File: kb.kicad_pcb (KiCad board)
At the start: 2 copper layers, 1 part, among them U1 Pico

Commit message: laid out LEDs
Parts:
- added C1: C_Small, Capacitor_SMD:C_0805_2012Metric_Pad1.18x1.45mm_HandSolder, B.Cu at (-240.5, 34.1)
- added C10: C_Small, Capacitor_SMD:C_0805_2012Metric_Pad1.18x1.45mm_HandSolder, B.Cu at (-28.2, 154.1)
- added C11: C_Small, Capacitor_SMD:C_0805_2012Metric_Pad1.18x1.45mm_HandSolder, B.Cu at (-178.3, 93.5)
- added C12: C_Small, Capacitor_SMD:C_0805_2012Metric_Pad1.18x1.45mm_HandSolder, B.Cu at (-229.1, 44.8)
- added C13: C_Small, Capacitor_SMD:C_0805_2012Metric_Pad1.18x1.45mm_HandSolder, B.Cu at (-256.1, 18.6)
- added C14: C_Small, Capacitor_SMD:C_0805_2012Metric_Pad1.18x1.45mm_HandSolder, B.Cu at (-224.3, 44.8)
- added C15: C_Small, Capacitor_SMD:C_0805_2012Metric_Pad1.18x1.45mm_HandSolder, B.Cu at (-121.2, 152.3)
- added C16: C_Small, Capacitor_SMD:C_0805_2012Metric_Pad1.18x1.45mm_HandSolder, B.Cu at (-220.2, 51.3)
- added C17: C_Small, Capacitor_SMD:C_0805_2012Metric_Pad1.18x1.45mm_HandSolder, B.Cu at (-178.3, 96.5)
- added C18: C_Small, Capacitor_SMD:C_0805_2012Metric_Pad1.18x1.45mm_HandSolder, B.Cu at (-151.2, 122.9)
- added C19: C_Small, Capacitor_SMD:C_0805_2012Metric_Pad1.18x1.45mm_HandSolder, B.Cu at (-191.8, 85.5)
- added C2: C_Small, Capacitor_SMD:C_0805_2012Metric_Pad1.18x1.45mm_HandSolder, B.Cu at (-180.3, 90.5)
- added C20: C_Small, Capacitor_SMD:C_0805_2012Metric_Pad1.18x1.45mm_HandSolder, B.Cu at (-235.8, 37.8)
- added C21: C_Small, Capacitor_SMD:C_0805_2012Metric_Pad1.18x1.45mm_HandSolder, B.Cu at (-173.5, 102.4)
- added C22: C_Small, Capacitor_SMD:C_0805_2012Metric_Pad1.18x1.45mm_HandSolder, B.Cu at (-18.5, 154.1)
- added C23: C_Small, Capacitor_SMD:C_0805_2012Metric_Pad1.18x1.45mm_HandSolder, B.Cu at (-129.0, 146.1)
- added C24: C_Small, Capacitor_SMD:C_0805_2012Metric_Pad1.18x1.45mm_HandSolder, B.Cu at (-205.9, 66.9)
- added C25: C_Small, Capacitor_SMD:C_0805_2012Metric_Pad1.18x1.45mm_HandSolder, B.Cu at (-159.9, 110.7)
- added C26: C_Small, Capacitor_SMD:C_0805_2012Metric_Pad1.18x1.45mm_HandSolder, B.Cu at (-23.3, 154.1)
- added C27: C_Small, Capacitor_SMD:C_0805_2012Metric_Pad1.18x1.45mm_HandSolder, B.Cu at (-153.3, 119.6)
- added C28: C_Small, Capacitor_SMD:C_0805_2012Metric_Pad1.18x1.45mm_HandSolder, B.Cu at (-191.8, 82.5)
- added C29: C_Small, Capacitor_SMD:C_0805_2012Metric_Pad1.18x1.45mm_HandSolder, B.Cu at (-240.5, 31.1)
- added C3: C_Small, Capacitor_SMD:C_0805_2012Metric_Pad1.18x1.45mm_HandSolder, B.Cu at (-159.9, 113.7)
- added C30: C_Small, Capacitor_SMD:C_0805_2012Metric_Pad1.18x1.45mm_HandSolder, B.Cu at (-164.7, 113.7)
- added C31: C_Small, Capacitor_SMD:C_0805_2012Metric_Pad1.18x1.45mm_HandSolder, B.Cu at (-144.5, 130.9)
- added C32: C_Small, Capacitor_SMD:C_0805_2012Metric_Pad1.18x1.45mm_HandSolder, B.Cu at (-164.7, 110.7)
- added C33: C_Small, Capacitor_SMD:C_0805_2012Metric_Pad1.18x1.45mm_HandSolder, B.Cu at (-173.5, 96.3)
- added C34: C_Small, Capacitor_SMD:C_0805_2012Metric_Pad1.18x1.45mm_HandSolder, B.Cu at (-205.9, 69.9)
- added C35: C_Small, Capacitor_SMD:C_0805_2012Metric_Pad1.18x1.45mm_HandSolder, B.Cu at (-173.5, 99.3)
- added C36: C_Small, Capacitor_SMD:C_0805_2012Metric_Pad1.18x1.45mm_HandSolder, B.Cu at (-145.5, 127.5)
- added C37: C_Small, Capacitor_SMD:C_0805_2012Metric_Pad1.18x1.45mm_HandSolder, B.Cu at (-185.1, 90.5)
- added C38: C_Small, Capacitor_SMD:C_0805_2012Metric_Pad1.18x1.45mm_HandSolder, B.Cu at (-129.0, 143.1)
- added C39: C_Small, Capacitor_SMD:C_0805_2012Metric_Pad1.18x1.45mm_HandSolder, B.Cu at (-200.2, 74.5)
- added C4: C_Small, Capacitor_SMD:C_0805_2012Metric_Pad1.18x1.45mm_HandSolder, B.Cu at (-215.8, 59.3)
- added C40: C_Small, Capacitor_SMD:C_0805_2012Metric_Pad1.18x1.45mm_HandSolder, B.Cu at (-200.2, 71.5)
- added C41: C_Small, Capacitor_SMD:C_0805_2012Metric_Pad1.18x1.45mm_HandSolder, B.Cu at (-139.7, 133.9)
- added C42: C_Small, Capacitor_SMD:C_0805_2012Metric_Pad1.18x1.45mm_HandSolder, B.Cu at (-183.1, 93.5)
- added C43: C_Small, Capacitor_SMD:C_0805_2012Metric_Pad1.18x1.45mm_HandSolder, B.Cu at (-246.2, 29.5)
- added C44: C_Small, Capacitor_SMD:C_0805_2012Metric_Pad1.18x1.45mm_HandSolder, B.Cu at (-246.2, 26.5)
- added C5: C_Small, Capacitor_SMD:C_0805_2012Metric_Pad1.18x1.45mm_HandSolder, B.Cu at (-186.0, 87.1)
- added C6: C_Small, Capacitor_SMD:C_0805_2012Metric_Pad1.18x1.45mm_HandSolder, B.Cu at (-165.7, 107.6)
- added C7: C_Small, Capacitor_SMD:C_0805_2012Metric_Pad1.18x1.45mm_HandSolder, B.Cu at (-139.7, 130.9)
- added C8: C_Small, Capacitor_SMD:C_0805_2012Metric_Pad1.18x1.45mm_HandSolder, B.Cu at (-138.8, 139.8)
- added C9: C_Small, Capacitor_SMD:C_0805_2012Metric_Pad1.18x1.45mm_HandSolder, B.Cu at (-228.0, 47.8)
- added D0: D_Small, Diode_SMD:D_SOD-123, B.Cu at (-230.5, 38.2)
- added D1: D_Small, Diode_SMD:D_SOD-123, B.Cu at (-209.2, 52.8)
- added D10: D_Small, Diode_SMD:D_SOD-123, B.Cu at (-140.2, 127.7)
- added D101: SK6812MINI, Keebio-Parts:SK6812-MINI-E, B.Cu at (56.4, 77.0)
- added D102: SK6812MINI, Keebio-Parts:SK6812-MINI-E, B.Cu at (75.4, 77.0)
- added D103: SK6812MINI, Keebio-Parts:SK6812-MINI-E, B.Cu at (99.2, 77.0)
- added D104: SK6812MINI, Keebio-Parts:SK6812-MINI-E, B.Cu at (118.3, 77.0)
- added D105: SK6812MINI, Keebio-Parts:SK6812-MINI-E, B.Cu at (137.3, 77.0)
- added D106: SK6812MINI, Keebio-Parts:SK6812-MINI-E, B.Cu at (156.4, 77.0)
- added D107: SK6812MINI, Keebio-Parts:SK6812-MINI-E, B.Cu at (175.4, 77.0)
- added D108: SK6812MINI, Keebio-Parts:SK6812-MINI-E, B.Cu at (194.5, 77.0)
- added D109: SK6812MINI, Keebio-Parts:SK6812-MINI-E, B.Cu at (37.3, 96.0)
- added D11: D_Small, Diode_SMD:D_SOD-123, B.Cu at (-123.8, 144.5)
- added D110: SK6812MINI, Keebio-Parts:SK6812-MINI-E, B.Cu at (56.4, 96.0)
- added D111: SK6812MINI, Keebio-Parts:SK6812-MINI-E, B.Cu at (75.4, 96.0)
- added D112: SK6812MINI, Keebio-Parts:SK6812-MINI-E, B.Cu at (104.0, 96.0)
- added D113: SK6812MINI, Keebio-Parts:SK6812-MINI-E, B.Cu at (127.8, 96.0)
- added D114: SK6812MINI, Keebio-Parts:SK6812-MINI-E, B.Cu at (146.8, 96.0)
- added D115: SK6812MINI, Keebio-Parts:SK6812-MINI-E, B.Cu at (165.9, 96.0)
- added D116: SK6812MINI, Keebio-Parts:SK6812-MINI-E, B.Cu at (184.9, 96.0)
- added D117: SK6812MINI, Keebio-Parts:SK6812-MINI-E, B.Cu at (204.0, 96.0)
- added D118: SK6812MINI, Keebio-Parts:SK6812-MINI-E, B.Cu at (37.3, 115.1)
- added D119: SK6812MINI, Keebio-Parts:SK6812-MINI-E, B.Cu at (56.4, 115.1)
- added D12: D_Small, Diode_SMD:D_SOD-123, B.Cu at (-146.0, 124.3)
- added D120: SK6812MINI, Keebio-Parts:SK6812-MINI-E, B.Cu at (75.4, 115.1)
- added D121: SK6812MINI, Keebio-Parts:SK6812-MINI-E, B.Cu at (106.4, 115.1)
- added D122: SK6812MINI, Keebio-Parts:SK6812-MINI-E, B.Cu at (132.6, 115.1)
- added D123: SK6812MINI, Keebio-Parts:SK6812-MINI-E, B.Cu at (151.6, 115.1)
- added D124: SK6812MINI, Keebio-Parts:SK6812-MINI-E, B.Cu at (170.7, 115.1)
- added D125: SK6812MINI, Keebio-Parts:SK6812-MINI-E, B.Cu at (189.7, 115.1)
- added D126: SK6812MINI, Keebio-Parts:SK6812-MINI-E, B.Cu at (208.8, 115.1)
- added D127: SK6812MINI, Keebio-Parts:SK6812-MINI-E, B.Cu at (37.3, 134.1)
- added D128: SK6812MINI, Keebio-Parts:SK6812-MINI-E, B.Cu at (56.4, 134.1)
- added D129: SK6812MINI, Keebio-Parts:SK6812-MINI-E, B.Cu at (75.4, 134.1)
- added D13: D_Small, Diode_SMD:D_SOD-123, B.Cu at (-168.2, 101.1)
- added D130: SK6812MINI, Keebio-Parts:SK6812-MINI-E, B.Cu at (111.1, 134.1)
- added D131: SK6812MINI, Keebio-Parts:SK6812-MINI-E, B.Cu at (142.1, 134.1)
- added D132: SK6812MINI, Keebio-Parts:SK6812-MINI-E, B.Cu at (161.1, 134.1)
- added D133: SK6812MINI, Keebio-Parts:SK6812-MINI-E, B.Cu at (180.2, 134.1)
- added D134: SK6812MINI, Keebio-Parts:SK6812-MINI-E, B.Cu at (199.2, 134.1)
- added D135: SK6812MINI, Keebio-Parts:SK6812-MINI-E, B.Cu at (218.3, 134.1)
- added D136: SK6812MINI, Keebio-Parts:SK6812-MINI-E, B.Cu at (37.3, 153.2)
- added D137: SK6812MINI, Keebio-Parts:SK6812-MINI-E, B.Cu at (56.4, 153.2)
- added D138: SK6812MINI, Keebio-Parts:SK6812-MINI-E, B.Cu at (75.4, 153.2)
- added D139: SK6812MINI, Keebio-Parts:SK6812-MINI-E, B.Cu at (104.0, 153.2)
- added D14: D_Small, Diode_SMD:D_SOD-123, B.Cu at (-168.2, 97.8)
- added D140: SK6812MINI, Keebio-Parts:SK6812-MINI-E, B.Cu at (130.2, 153.2)
- added D141: SK6812MINI, Keebio-Parts:SK6812-MINI-E, B.Cu at (154.0, 153.2)
- added D142: SK6812MINI, Keebio-Parts:SK6812-MINI-E, B.Cu at (177.8, 153.2)
- added D143: SK6812MINI, Keebio-Parts:SK6812-MINI-E, B.Cu at (208.8, 153.2)
- added D144: SK6812MINI, Keebio-Parts:SK6812-MINI-E, B.Cu at (213.5, 77.0)
- added D15: D_Small, Diode_SMD:D_SOD-123, B.Cu at (-140.2, 124.3)
- added D16: D_Small, Diode_SMD:D_SOD-123, B.Cu at (-173.0, 93.2)
- added D17: D_Small, Diode_SMD:D_SOD-123, B.Cu at (-116.0, 152.5)
- added D18: D_Small, Diode_SMD:D_SOD-123, B.Cu at (-127.8, 139.9)
- added D19: D_Small, Diode_SMD:D_SOD-123, B.Cu at (-235.2, 31.3)
- added D2: D_Small, Diode_SMD:D_SOD-123, B.Cu at (-186.5, 83.9)
- added D20: D_Small, Diode_SMD:D_SOD-123, B.Cu at (-230.5, 41.6)
- added D21: D_Small, Diode_SMD:D_SOD-123, B.Cu at (-214.9, 52.8)
- added D22: D_Small, Diode_SMD:D_SOD-123, B.Cu at (-116.0, 149.1)
- added D23: D_Small, Diode_SMD:D_SOD-123, B.Cu at (-235.2, 27.9)
- added D24: D_Small, Diode_SMD:D_SOD-123, B.Cu at (-180.8, 83.9)
- added D25: D_Small, Diode_SMD:D_SOD-123, B.Cu at (-180.8, 87.3)
- added D26: D_Small, Diode_SMD:D_SOD-123, B.Cu at (-210.5, 56.1)
- added D27: D_Small, Diode_SMD:D_SOD-123, B.Cu at (-222.7, 48.1)
- added D28: D_Small, Diode_SMD:D_SOD-123, B.Cu at (-217.0, 48.1)
- added D29: D_Small, Diode_SMD:D_SOD-123, B.Cu at (-133.6, 139.9)
- added D3: D_Small, Diode_SMD:D_SOD-123, B.Cu at (-160.4, 107.5)
- added D30: D_Small, Diode_SMD:D_SOD-123, B.Cu at (-216.2, 56.1)
- added D31: D_Small, Diode_SMD:D_SOD-123, B.Cu at (-194.9, 78.4)
- added D32: D_Small, Diode_SMD:D_SOD-123, B.Cu at (-166.2, 104.5)
- added D33: D_Small, Diode_SMD:D_SOD-123, B.Cu at (-250.8, 22.1)
- added D34: D_Small, Diode_SMD:D_SOD-123, B.Cu at (-188.6, 79.3)
- added D35: D_Small, Diode_SMD:D_SOD-123, B.Cu at (-235.2, 34.6)
- added D36: D_Small, Diode_SMD:D_SOD-123, B.Cu at (-148.0, 119.7)
- added D37: D_Small, Diode_SMD:D_SOD-123, B.Cu at (-160.4, 104.1)
- added D38: D_Small, Diode_SMD:D_SOD-123, B.Cu at (-194.9, 75.0)
- added D39: D_Small, Diode_SMD:D_SOD-123, B.Cu at (-241.0, 27.9)
- added D4: D_Small, Diode_SMD:D_SOD-123, B.Cu at (-200.6, 68.3)
- added D40: D_Small, Diode_SMD:D_SOD-123, B.Cu at (-250.8, 18.7)
- added D41: D_Small, Diode_SMD:D_SOD-123, B.Cu at (-210.5, 59.5)
- added D42: D_Small, Diode_SMD:D_SOD-123, B.Cu at (-224.8, 41.6)
- added D43: D_Small, Diode_SMD:D_SOD-123, B.Cu at (-224.8, 38.2)
- added D44: D_Small, Diode_SMD:D_SOD-123, B.Cu at (-202.7, 63.7)
- added D5: D_Small, Diode_SMD:D_SOD-123, B.Cu at (-194.9, 71.7)
- added D6: D_Small, Diode_SMD:D_SOD-123, B.Cu at (-243.0, 23.3)
- added D7: D_Small, Diode_SMD:D_SOD-123, B.Cu at (-210.5, 62.8)
- added D8: D_Small, Diode_SMD:D_SOD-123, B.Cu at (-121.7, 149.1)
- added D9: D_Small, Diode_SMD:D_SOD-123, B.Cu at (-194.9, 68.3)
- added J1: Conn_01x04_Female, Connector_PinSocket_2.54mm:PinSocket_1x04_P2.54mm_Vertical, F.Cu at (-53.2, -29.2)
- added J2: 10029449-001RLF, 10029449-001RLF:AMPHENOL_10029449-001RLF, B.Cu at (-25.7, 143.3)
- added MX1: MX-NoLED, MX_Only:MXOnly-1U-Hotswap, F.Cu at (56.4, 71.4)
- added MX10: MX-NoLED, MX_Only:MXOnly-1U-Hotswap, F.Cu at (56.4, 90.5)
- added MX11: MX-NoLED, MX_Only:MXOnly-1U-Hotswap, F.Cu at (75.4, 90.5)
- added MX12: MX-NoLED, MX_Only:MXOnly-1.5U-Hotswap, F.Cu at (104.0, 90.5)
- added MX13: MX-NoLED, MX_Only:MXOnly-1U-Hotswap, F.Cu at (127.8, 90.5)
- added MX14: MX-NoLED, MX_Only:MXOnly-1U-Hotswap, F.Cu at (146.8, 90.5)
- added MX15: MX-NoLED, MX_Only:MXOnly-1U-Hotswap, F.Cu at (165.9, 90.5)
- added MX16: MX-NoLED, MX_Only:MXOnly-1U-Hotswap, F.Cu at (184.9, 90.5)
- added MX17: MX-NoLED, MX_Only:MXOnly-1U-Hotswap, F.Cu at (204.0, 90.5)
- added MX18: MX-NoLED, MX_Only:MXOnly-1U-Hotswap, F.Cu at (37.3, 109.5)
- added MX19: MX-NoLED, MX_Only:MXOnly-1U-Hotswap, F.Cu at (56.4, 109.5)
- added MX2: MX-NoLED, MX_Only:MXOnly-1U-Hotswap, F.Cu at (75.4, 71.4)
- added MX20: MX-NoLED, MX_Only:MXOnly-1U-Hotswap, F.Cu at (75.4, 109.5)
- added MX21: MX-NoLED, MX_Only:MXOnly-1.75U-Hotswap, F.Cu at (106.4, 109.5)
- added MX22: MX-NoLED, MX_Only:MXOnly-1U-Hotswap, F.Cu at (132.6, 109.5)
- added MX23: MX-NoLED, MX_Only:MXOnly-1U-Hotswap, F.Cu at (151.6, 109.5)
- added MX24: MX-NoLED, MX_Only:MXOnly-1U-Hotswap, F.Cu at (170.7, 109.5)
- added MX25: MX-NoLED, MX_Only:MXOnly-1U-Hotswap, F.Cu at (189.7, 109.5)
- added MX26: MX-NoLED, MX_Only:MXOnly-1U-Hotswap, F.Cu at (208.8, 109.5)
- added MX27: MX-NoLED, MX_Only:MXOnly-1U-Hotswap, F.Cu at (37.3, 128.6)
- added MX28: MX-NoLED, MX_Only:MXOnly-1U-Hotswap, F.Cu at (56.4, 128.6)
- added MX29: MX-NoLED, MX_Only:MXOnly-1U-Hotswap, F.Cu at (75.4, 128.6)
- added MX3: MX-NoLED, MX_Only:MXOnly-1U-Hotswap, F.Cu at (99.2, 71.4)
- added MX30: MX-NoLED, MX_Only:MXOnly-2.25U-Hotswap, F.Cu at (111.1, 128.6)
- added MX31: MX-NoLED, MX_Only:MXOnly-1U-Hotswap, F.Cu at (142.1, 128.6)
- added MX32: MX-NoLED, MX_Only:MXOnly-1U-Hotswap, F.Cu at (161.1, 128.6)
- added MX33: MX-NoLED, MX_Only:MXOnly-1U-Hotswap, F.Cu at (180.2, 128.6)
- added MX34: MX-NoLED, MX_Only:MXOnly-1U-Hotswap, F.Cu at (199.2, 128.6)
- added MX35: MX-NoLED, MX_Only:MXOnly-1U-Hotswap, F.Cu at (218.3, 128.6)
- added MX36: MX-NoLED, MX_Only:MXOnly-1U-Hotswap, F.Cu at (37.3, 147.6)
- added MX37: MX-NoLED, MX_Only:MXOnly-1U-Hotswap, F.Cu at (56.4, 147.6)
- added MX38: MX-NoLED, MX_Only:MXOnly-1U-Hotswap, F.Cu at (75.4, 147.6)
- added MX39: MX-NoLED, MX_Only:MXOnly-1.5U-Hotswap, F.Cu at (104.0, 147.6)
- added MX4: MX-NoLED, MX_Only:MXOnly-1U-Hotswap, F.Cu at (118.3, 71.4)
- added MX40: MX-NoLED, MX_Only:MXOnly-1.25U-Hotswap, F.Cu at (130.2, 147.6)
- added MX41: MX-NoLED, MX_Only:MXOnly-1.25U-Hotswap, F.Cu at (154.0, 147.6)
- added MX42: MX-NoLED, MX_Only:MXOnly-1.25U-Hotswap, F.Cu at (177.8, 147.6)
- added MX43: MX-NoLED, MX_Only:MXOnly-2U-Hotswap, F.Cu at (208.8, 147.6)
- added MX44: MX-NoLED, MX_Only:MXOnly-1U-Hotswap, F.Cu at (213.5, 71.4)
- added MX5: MX-NoLED, MX_Only:MXOnly-1U-Hotswap, F.Cu at (137.3, 71.4)
- added MX6: MX-NoLED, MX_Only:MXOnly-1U-Hotswap, F.Cu at (156.4, 71.4)
- added MX7: MX-NoLED, MX_Only:MXOnly-1U-Hotswap, F.Cu at (175.4, 71.4)
- added MX8: MX-NoLED, MX_Only:MXOnly-1U-Hotswap, F.Cu at (194.5, 71.4)
- added MX9: MX-NoLED, MX_Only:MXOnly-1U-Hotswap, F.Cu at (37.3, 90.5)
- added SW1: RotaryEncoder_Switch, Keebio-Parts:RotaryEncoder_EC11, F.Cu at (33.3, 67.5)
- added U2: SN74AHCT125D, Package_DIP:DIP-14_W7.62mm_Socket, F.Cu at (-71.3, -33.8)
- moved U1 30.2 mm to (49.2, 25.4), turned to 90 degrees
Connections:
- U1 pad 13: unconnected-(U1-Pad13) -> GND
- U1 pad 18: unconnected-(U1-Pad18) -> GND
- U1 pad 3: unconnected-(U1-Pad3) -> GND
- U1 pad 40: unconnected-(U1-Pad40) -> +5V
- U1 pad 42: unconnected-(U1-Pad42) -> GND
- U1 pad 8: unconnected-(U1-Pad8) -> GND
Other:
- board outline added: 3.4 x 3 mm

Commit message: layout nearly finished
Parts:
- U1: moved to B.Cu
- moved D35 471.3 mm to (225.4, 134.1), turned to 90 degrees
- moved C43 464.6 mm to (201.6, 153.2), turned to 90 degrees
- moved D43 455.4 mm to (215.9, 153.2), turned to 90 degrees
- moved C44 455.4 mm to (206.4, 77.0), turned to 90 degrees
- moved D33 452.2 mm to (187.3, 134.1), turned to 90 degrees
- moved D26 430.4 mm to (215.9, 115.1), turned to 90 degrees
- moved D42 424.6 mm to (184.9, 153.2), turned to 90 degrees
- moved D44 423.6 mm to (220.7, 77.0), turned to 90 degrees
- moved D40 410.8 mm to (137.3, 153.2), turned to 90 degrees
- moved D6 410.0 mm to (163.5, 77.0), turned to 90 degrees
- moved D23 403.5 mm to (158.8, 115.1), turned to 90 degrees
- moved C34 403.1 mm to (192.1, 134.1), turned to 90 degrees
- moved C16 400.5 mm to (177.8, 96.0), turned to 90 degrees
- moved D34 398.7 mm to (206.4, 134.1), turned to 90 degrees
- moved D7 393.3 mm to (182.6, 77.0), turned to 90 degrees
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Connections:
- D103 pad 1: Net-(D103-Pad1) -> (no net)
- D103 pad 2: GND -> (no net)
- D103 pad 3: Net-(D102-Pad1) -> (no net)
- D103 pad 4: +5V -> (no net)
- D115 pad 1: Net-(D115-Pad1) -> (no net)
- D115 pad 2: GND -> (no net)
- D115 pad 3: Net-(D114-Pad1) -> (no net)
- D115 pad 4: +5V -> (no net)
- D29 pad 1: /ROW3 -> (no net)
- D29 pad 2: Net-(MX29-Pad2) -> (no net)
- D34 pad 1: /ROW3 -> (no net)
- D34 pad 2: Net-(MX34-Pad2) -> (no net)
- MX9 pad 1: /COL0 -> (no net)
- MX9 pad 2: Net-(MX9-Pad2) -> (no net)

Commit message: about to start routing
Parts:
- U2: footprint Package_DIP:DIP-14_W7.62mm_Socket -> Package_SO:TSSOP-14-1EP_4.4x5mm_P0.65mm; moved to B.Cu
- moved U1 40.5 mm to (61.9, 66.7)
- moved U2 13.2 mm to (77.8, 44.5), turned to 180 degrees
- moved J2 2.30 mm to (101.2, 52.4), turned to -90 degrees
- moved C1 1.59 mm to (49.2, 70.6)
- moved C2 1.59 mm to (68.3, 70.6)
- moved D0 1.59 mm to (44.5, 70.6)
- moved D1 1.59 mm to (63.5, 70.6)
- moved D2 1.59 mm to (82.5, 70.6)
- moved J1 0.79 mm to (91.3, 52.2)
- turned SW1 to 180 degrees
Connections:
- D101 pad 3: unconnected-(D101-Pad3) -> /RGB_5V
- D103 pad 1: (no net) -> Net-(D103-Pad1)
- D103 pad 2: (no net) -> GND
- D103 pad 3: (no net) -> Net-(D102-Pad1)
- D103 pad 4: (no net) -> +5V
- D108 pad 1: unconnected-(D108-Pad1) -> Net-(D109-Pad3)
- D109 pad 3: unconnected-(D109-Pad3) -> Net-(D109-Pad3)
- D115 pad 1: (no net) -> Net-(D115-Pad1)
- D115 pad 2: (no net) -> GND
- D115 pad 3: (no net) -> Net-(D114-Pad1)
- D115 pad 4: (no net) -> +5V
- D117 pad 1: unconnected-(D117-Pad1) -> Net-(D118-Pad3)
- D118 pad 3: unconnected-(D118-Pad3) -> Net-(D118-Pad3)
- D126 pad 1: unconnected-(D126-Pad1) -> Net-(D127-Pad3)
- D127 pad 3: unconnected-(D127-Pad3) -> Net-(D127-Pad3)
- D135 pad 1: unconnected-(D135-Pad1) -> Net-(D136-Pad3)
- D136 pad 3: unconnected-(D136-Pad3) -> Net-(D136-Pad3)
- D144 pad 1: unconnected-(D144-Pad1) -> /RGB_TO_RIGHT
- D29 pad 1: (no net) -> /ROW3
- D29 pad 2: (no net) -> Net-(D29-Pad2)
- D34 pad 1: (no net) -> /ROW3
- D34 pad 2: (no net) -> Net-(D34-Pad2)
- D9 pad 2: Net-(MX9-Pad2) -> Net-(D9-Pad2)
- MX29 pad 2: Net-(MX29-Pad2) -> Net-(D29-Pad2)
- MX34 pad 2: Net-(MX34-Pad2) -> Net-(D34-Pad2)
- MX9 pad 1: (no net) -> /COL0
- MX9 pad 2: (no net) -> Net-(D9-Pad2)

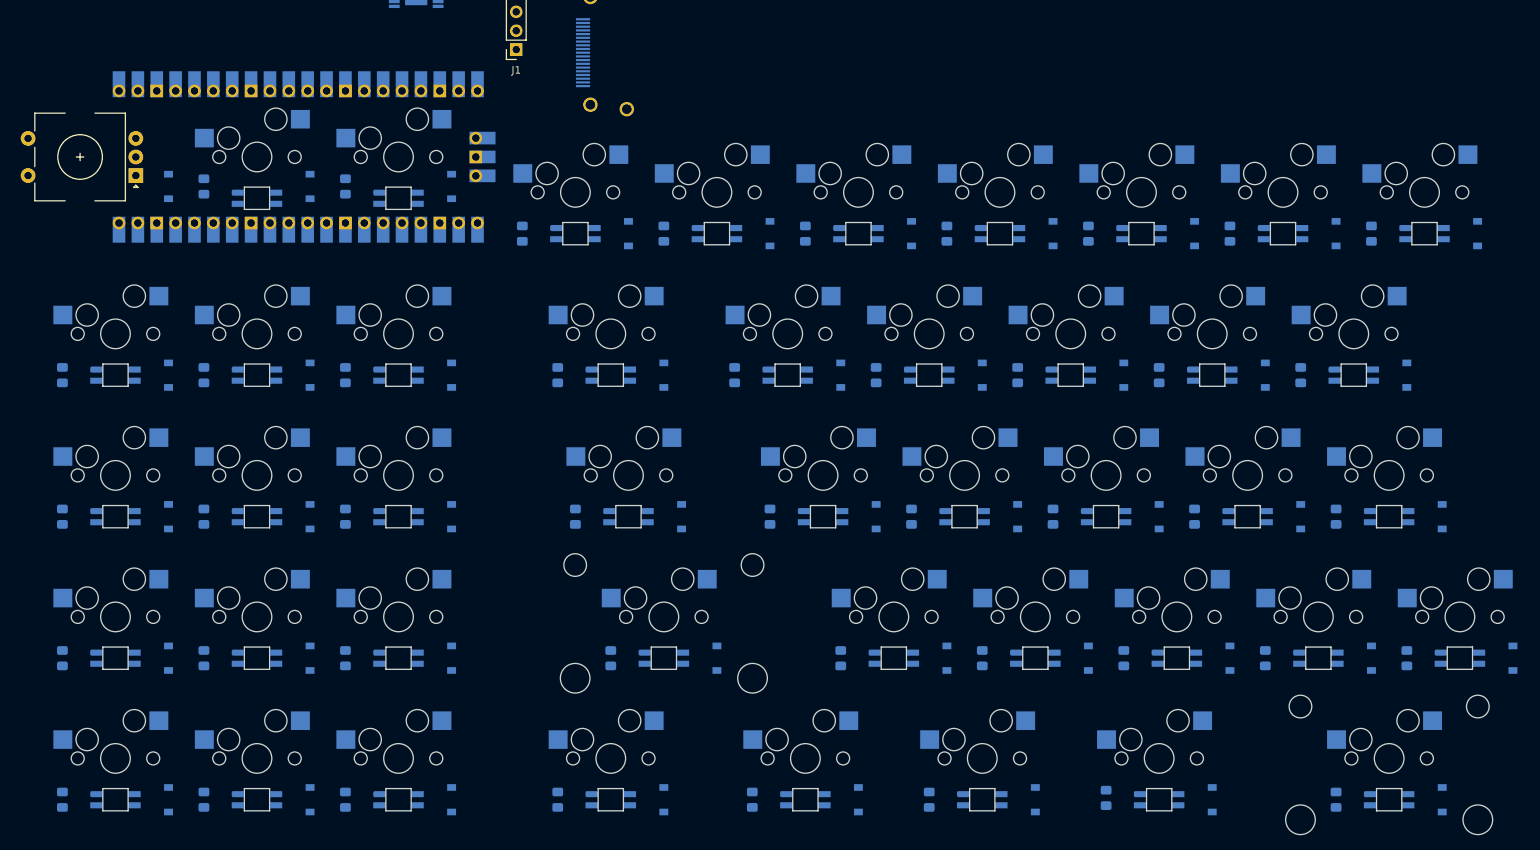
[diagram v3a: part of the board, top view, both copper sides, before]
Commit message: cols 3-8 done
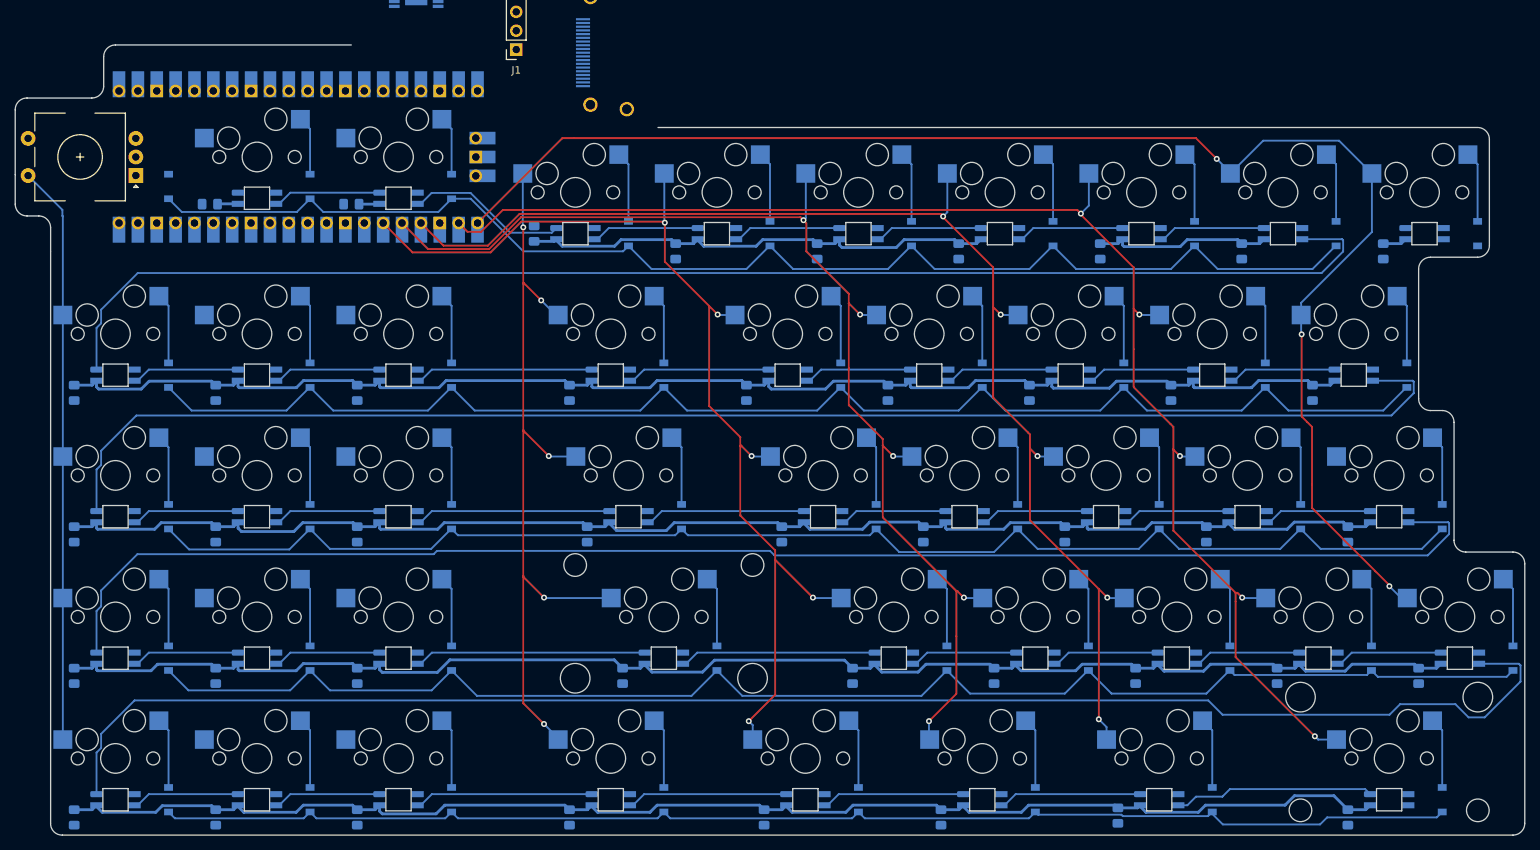
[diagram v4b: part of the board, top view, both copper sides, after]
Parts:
- MX43: footprint MX_Only:MXOnly-2U-Hotswap -> MX_Only:MXOnly-2U-Hotswap-ReversedStabilizers
- moved C42 2.86 mm to (172.2, 155.3), turned to -90 degrees
- moved C14 2.86 mm to (141.3, 98.4), turned to -90 degrees
- moved C15 2.86 mm to (160.3, 98.4), turned to -90 degrees
- moved C17 2.86 mm to (198.4, 98.4), turned to -90 degrees
- moved C21 2.86 mm to (100.8, 117.5), turned to -90 degrees
- moved C22 2.86 mm to (127.0, 117.5), turned to -90 degrees
- moved C23 2.86 mm to (146.1, 117.5), turned to -90 degrees
- moved C24 2.86 mm to (165.1, 117.5), turned to -90 degrees
- moved C25 2.86 mm to (184.2, 117.5), turned to -90 degrees
- moved C31 2.86 mm to (136.5, 136.5), turned to -90 degrees
- moved C33 2.86 mm to (174.6, 136.5), turned to -90 degrees
- moved C34 2.86 mm to (193.7, 136.5), turned to -90 degrees
- moved C35 2.86 mm to (212.7, 136.5), turned to -90 degrees
- moved C4 2.86 mm to (112.7, 79.4), turned to -90 degrees
- moved C40 2.86 mm to (124.6, 155.6), turned to -90 degrees
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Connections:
- SW1 pad S1: /COL0 -> Net-(D0-Pad2)
- SW1 pad S2: Net-(D0-Pad2) -> /COL0
- U1 pad 21: unconnected-(U1-Pad21) -> /COL8
- U1 pad 22: unconnected-(U1-Pad22) -> /COL7
- U1 pad 23: unconnected-(U1-Pad23) -> GND
- U1 pad 24: unconnected-(U1-Pad24) -> /COL6
- U1 pad 25: unconnected-(U1-Pad25) -> /COL5
- U1 pad 26: unconnected-(U1-Pad26) -> /COL4
- U1 pad 27: unconnected-(U1-Pad27) -> /COL3
- U1 pad 28: unconnected-(U1-Pad28) -> GND
- U1 pad 29: unconnected-(U1-Pad29) -> /COL2
- U1 pad 31: unconnected-(U1-Pad31) -> /COL1
- U1 pad 32: unconnected-(U1-Pad32) -> /COL0
- U1 pad 33: unconnected-(U1-Pad33) -> GND
- U1 pad 38: unconnected-(U1-Pad38) -> GND
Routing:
- net +5V: track 0.00 -> 852.6 mm
- net Net-(D135-Pad1): track 0.00 -> 213.3 mm
- net Net-(D126-Pad1): track 0.00 -> 200.8 mm
- net /COL8: track 0.00 -> 198.3 mm, vias 0 -> 3
- net /ROW3: track 0.00 -> 197.5 mm
- net Net-(D117-Pad1): track 0.00 -> 195.4 mm
- net /COL7: track 0.00 -> 189.5 mm, vias 0 -> 5
- net /ROW1: track 0.00 -> 187.3 mm
- net /ROW2: track 0.00 -> 186.6 mm
- net Net-(D108-Pad1): track 0.00 -> 185.9 mm
- net /ROW4: track 0.00 -> 177.0 mm
- net /ROW0: track 0.00 -> 176.2 mm
- net /COL6: track 0.00 -> 170.4 mm, vias 0 -> 5
- net /COL5: track 0.00 -> 156.7 mm, vias 0 -> 5
- net /COL4: track 0.00 -> 145.1 mm, vias 0 -> 5
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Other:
- board size 3.4 x 3 mm -> 203.2 x 106.4 mm

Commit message: before rgb restructure
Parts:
- moved U2 38.4 mm to (44.2, 63.1), turned to -90 degrees
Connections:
- J1 pad 2: +5V -> +3V3
- J2 pad 15: unconnected-(J2-Pad15) -> /ENC_R1
- J2 pad 16: unconnected-(J2-Pad16) -> /ENC_R2
- J2 pad 19: unconnected-(J2-Pad19) -> /RGB_TO_RIGHT
- U1 pad 1: unconnected-(U1-Pad1) -> /ENC_L2
- U1 pad 19: unconnected-(U1-Pad19) -> /ENC_R1
- U1 pad 2: unconnected-(U1-Pad2) -> /RGB_3V3
- U1 pad 20: unconnected-(U1-Pad20) -> /ENC_R2
- U1 pad 34: unconnected-(U1-Pad34) -> /ENC_L1
- U1 pad 36: unconnected-(U1-Pad36) -> +3V3
- U1 pad 4: unconnected-(U1-Pad4) -> /OLED_SDA
- U1 pad 5: unconnected-(U1-Pad5) -> /OLED_SCL
- U2 pad 2: /RGB_3V3 -> GND
- U2 pad 3: /RGB_5V -> unconnected-(U2-Pad3)
- U2 pad 8: unconnected-(U2-Pad8) -> /RGB_5V
- U2 pad 9: GND -> /RGB_3V3
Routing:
- net /RGB_TO_RIGHT: track 0.00 -> 139.9 mm
- net +5V: track 852.6 -> 968.5 mm
- net /COL1: track 0.00 -> 107.0 mm, vias 0 -> 5
- net /COL2: track 0.00 -> 94.8 mm, vias 0 -> 5
- net /COL0: track 77.9 -> 119.6 mm, vias 0 -> 4
- net Net-(D0-Pad2): track 0.00 -> 22.2 mm
- net /ENC_L1: track 0.00 -> 15.6 mm
- net /RGB_3V3: track 0.00 -> 12.2 mm
- net /RGB_5V: track 0.00 -> 9.90 mm
- net /ENC_L2: track 0.00 -> 7.33 mm
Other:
- outline, holes or cut-outs redrawn

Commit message: relaying out?
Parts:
- moved J1 3.81 mm to (87.6, 51.1)
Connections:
- D109 pad 3: Net-(D108-Pad1) -> Net-(D109-Pad3)
- D143 pad 1: Net-(D143-Pad1) -> /RGB_TO_RIGHT
- D144 pad 1: /RGB_TO_RIGHT -> Net-(D109-Pad3)
- D144 pad 3: Net-(D143-Pad1) -> Net-(D108-Pad1)
- U1 pad 1: /ENC_L2 -> /ENC_L1
- U1 pad 10: unconnected-(U1-Pad10) -> /ENC_R2
- U1 pad 11: unconnected-(U1-Pad11) -> /ENC_R1
- U1 pad 12: unconnected-(U1-Pad12) -> /COL2
- U1 pad 14: unconnected-(U1-Pad14) -> /COL3
- U1 pad 15: unconnected-(U1-Pad15) -> /COL4
- U1 pad 16: unconnected-(U1-Pad16) -> /COL5
- U1 pad 17: unconnected-(U1-Pad17) -> /COL6
- U1 pad 19: /ENC_R1 -> /COL7
- U1 pad 2: /RGB_3V3 -> /ENC_L2
- U1 pad 20: /ENC_R2 -> /COL8
- U1 pad 21: /COL8 -> unconnected-(U1-Pad21)
- U1 pad 22: /COL7 -> unconnected-(U1-Pad22)
- U1 pad 24: /COL6 -> unconnected-(U1-Pad24)
- U1 pad 25: /COL5 -> unconnected-(U1-Pad25)
- U1 pad 26: /COL4 -> unconnected-(U1-Pad26)
- U1 pad 27: /COL3 -> /ROW4
- U1 pad 29: /COL2 -> /ROW3
- U1 pad 31: /COL1 -> /ROW2
- U1 pad 32: /COL0 -> /ROW1
- U1 pad 34: /ENC_L1 -> /ROW0
- U1 pad 4: /OLED_SDA -> /RGB_3V3
- U1 pad 5: /OLED_SCL -> /COL0
- U1 pad 6: unconnected-(U1-Pad6) -> /OLED_SDA
- U1 pad 7: unconnected-(U1-Pad7) -> /OLED_SCL
- U1 pad 9: unconnected-(U1-Pad9) -> /COL1
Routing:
- net Net-(D109-Pad3): track 0.00 -> 193.3 mm
- net Net-(D108-Pad1): track 185.9 -> 14.6 mm
- net /ROW4: track 177.0 -> 266.3 mm, vias 0 -> 2
- net /RGB_TO_RIGHT: track 139.9 -> 199.5 mm, vias 0 -> 2
- net /COL4: track 145.1 -> 123.1 mm
- net /COL5: track 156.7 -> 137.5 mm
- net +5V: track 968.5 -> 986.0 mm
- net /COL6: track 170.4 -> 154.1 mm
- net /COL8: track 198.3 -> 189.2 mm
- net Net-(D2-Pad2): track 7.94 -> 0.00 mm
- net /COL7: track 189.5 -> 181.8 mm
- net /COL2: track 94.8 -> 102.3 mm
- net /COL1: track 107.0 -> 102.7 mm, vias 5 -> 4
- net /COL0: track 119.6 -> 115.9 mm
- net /ENC_L1: track 15.6 -> 12.3 mm
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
